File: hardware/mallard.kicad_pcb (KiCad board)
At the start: 2 copper layers, 70 parts, among them J1 USB_A, J2 Conn_02x03_Odd_Even, J3 Conn_01x03, SW1 RESET Switch, U1 TMP235, U10 LTC1983ES6-3, U11 STM32L4Q5xx, U2 TMP235, U3 TMP235, U4 BQ24210DQCT, U5 TMUX1309, U6 TMUX1309, U7 LMP7721, U8 TPS71710DRVR, U9 LMV554

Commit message: Schematic prepared for Layout
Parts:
- added SM1: Conn_01x03, Connector_PinHeader_2.54mm:PinHeader_1x03_P2.54mm_Vertical_SMD_Pin1Right, F.Cu at (24.8, 54.6)
- added SM2: Conn_01x03, Connector_PinHeader_2.54mm:PinHeader_1x03_P2.54mm_Vertical_SMD_Pin1Right, F.Cu at (32.7, 54.6)
- added SM3: Conn_01x03, Connector_PinHeader_2.54mm:PinHeader_1x03_P2.54mm_Vertical_SMD_Pin1Right, F.Cu at (40.7, 54.6)
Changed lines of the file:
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@@
     (tracks 0)
     (zones 0)
-    (modules 70)
+    (modules 73)
     (nets 102)
   )
@@
     (add_net USART1_TX)
   )
+  (module Connector_PinHeader_2.54mm:PinHeader_1x03_P2.54mm_Vertical_SMD_Pin1Right (layer F.Cu)
+    (at 40.665 54.61)
+    (descr "surface-mounted straight pin header, 1x03, 2.54mm pitch, single row, style 2 (pin 1 right)")
+    (tags "Surface mounted pin header SMD 1x03 2.54mm single row style2 pin1 right")
+    (attr smd)
+    (fp_text reference SM3 (at 0 -4.87) (layer F.SilkS)
+      (effects (font (size 1 1) (thickness 0.15)))
+    )
+    (fp_text value Conn_01x03 (at 0 4.87) (layer F.Fab)
+      (effects (font (size 1 1) (thickness 0.15)))
+    )
+    (fp_text user %R (at 0 0 90) (layer F.Fab)
+      (effects (font (size 1 1) (thickness 0.15)))
+    )
+    (fp_line (start 1.27 3.81) (end -1.27 3.81) (layer F.Fab) (width 0.1))
+    (fp_line (start -1.27 -3.81) (end 0.32 -3.81) (layer F.Fab) (width 0.1))
+    (fp_line (start 1.27 3.81) (end 1.27 -2.86) (layer F.Fab) (width 0.1))
+    (fp_line (start 1.27 -2.86) (end 0.32 -3.81) (layer F.Fab) (width 0.1))
+    (fp_line (start -1.27 -3.81) (end -1.27 3.81) (layer F.Fab) (width 0.1))
+    (fp_line (start -1.27 -0.32) (end -2.54 -0.32) (layer F.Fab) (width 0.1))
+    (fp_line (start -2.54 -0.32) (end -2.54 0.32) (layer F.Fab) (width 0.1))
+    (fp_line (start -2.54 0.32) (end -1.27 0.32) (layer F.Fab) (width 0.1))
+    (fp_line (start 1.27 -2.86) (end 2.54 -2.86) (layer F.Fab) (width 0.1))
+    (fp_line (start 2.54 -2.86) (end 2.54 -2.22) (layer F.Fab) (width 0.1))
+    (fp_line (start 2.54 -2.22) (end 1.27 -2.22) (layer F.Fab) (width 0.1))
+    (fp_line (start 1.27 2.22) (end 2.54 2.22) (layer F.Fab) (width 0.1))
+    (fp_line (start 2.54 2.22) (end 2.54 2.86) (layer F.Fab) (width 0.1))
+    (fp_line (start 2.54 2.86) (end 1.27 2.86) (layer F.Fab) (width 0.1))
+    (fp_line (start -1.33 -3.87) (end 1.33 -3.87) (layer F.SilkS) (width 0.12))
+    (fp_line (start -1.33 3.87) (end 1.33 3.87) (layer F.SilkS) (width 0.12))
+    (fp_line (start 1.33 -1.78) (end 1.33 1.78) (layer F.SilkS) (width 0.12))
+    (fp_line (start -1.33 -3.87) (end -1.33 -0.76) (layer F.SilkS) (width 0.12))
+    (fp_line (start 1.33 -3.3) (end 2.85 -3.3) (layer F.SilkS) (width 0.12))
+    (fp_line (start 1.33 -3.87) (end 1.33 -3.3) (layer F.SilkS) (width 0.12))
+    (fp_line (start -1.33 3.3) (end -1.33 3.87) (layer F.SilkS) (width 0.12))
+    (fp_line (start -1.33 0.76) (end -1.33 3.87) (layer F.SilkS) (width 0.12))
+    (fp_line (start -3.45 -4.35) (end -3.45 4.35) (layer F.CrtYd) (width 0.05))
+    (fp_line (start -3.45 4.35) (end 3.45 4.35) (layer F.CrtYd) (width 0.05))
+    (fp_line (start 3.45 4.35) (end 3.45 -4.35) (layer F.CrtYd) (width 0.05))
+    (fp_line (start 3.45 -4.35) (end -3.45 -4.35) (layer F.CrtYd) (width 0.05))
+    (pad 3 smd rect (at 1.655 2.54) (size 2.51 1) (layers F.Cu F.Paste F.Mask)
+      (net 1 GND))
+    (pad 1 smd rect (at 1.655 -2.54) (size 2.51 1) (layers F.Cu F.Paste F.Mask)
+      (net 2 +3V3))
+    (pad 2 smd rect (at -1.655 0) (size 2.51 1) (layers F.Cu F.Paste F.Mask)
+      (net 58 "Net-(SM3-Pad2)"))
+    (model ${KISYS3DMOD}/Connector_PinHeader_2.54mm.3dshapes/PinHeader_1x03_P2.54mm_Vertical_SMD_Pin1Right.wrl
+      (at (xyz 0 0 0))
+      (scale (xyz 1 1 1))
+      (rotate (xyz 0 0 0))
+    )
+  )
+  (module Connector_PinHeader_2.54mm:PinHeader_1x03_P2.54mm_Vertical_SMD_Pin1Right (layer F.Cu)
+    (at 32.715 54.61)
+    (descr "surface-mounted straight pin header, 1x03, 2.54mm pitch, single row, style 2 (pin 1 right)")
+    (tags "Surface mounted pin header SMD 1x03 2.54mm single row style2 pin1 right")
+    (attr smd)
+    (fp_text reference SM2 (at 0 -4.87) (layer F.SilkS)
+      (effects (font (size 1 1) (thickness 0.15)))
+    )
+    (fp_text value Conn_01x03 (at 0 4.87) (layer F.Fab)
+      (effects (font (size 1 1) (thickness 0.15)))
+    )
+    (fp_text user %R (at 0 0 90) (layer F.Fab)
+      (effects (font (size 1 1) (thickness 0.15)))
+    )
+    (fp_line (start 1.27 3.81) (end -1.27 3.81) (layer F.Fab) (width 0.1))
+    (fp_line (start -1.27 -3.81) (end 0.32 -3.81) (layer F.Fab) (width 0.1))
+    (fp_line (start 1.27 3.81) (end 1.27 -2.86) (layer F.Fab) (width 0.1))
+    (fp_line (start 1.27 -2.86) (end 0.32 -3.81) (layer F.Fab) (width 0.1))
+    (fp_line (start -1.27 -3.81) (end -1.27 3.81) (layer F.Fab) (width 0.1))
+    (fp_line (start -1.27 -0.32) (end -2.54 -0.32) (layer F.Fab) (width 0.1))
+    (fp_line (start -2.54 -0.32) (end -2.54 0.32) (layer F.Fab) (width 0.1))
+    (fp_line (start -2.54 0.32) (end -1.27 0.32) (layer F.Fab) (width 0.1))
+    (fp_line (start 1.27 -2.86) (end 2.54 -2.86) (layer F.Fab) (width 0.1))
+    (fp_line (start 2.54 -2.86) (end 2.54 -2.22) (layer F.Fab) (width 0.1))
+    (fp_line (start 2.54 -2.22) (end 1.27 -2.22) (layer F.Fab) (width 0.1))
+    (fp_line (start 1.27 2.22) (end 2.54 2.22) (layer F.Fab) (width 0.1))
+    (fp_line (start 2.54 2.22) (end 2.54 2.86) (layer F.Fab) (width 0.1))
+    (fp_line (start 2.54 2.86) (end 1.27 2.86) (layer F.Fab) (width 0.1))
+    (fp_line (start -1.33 -3.87) (end 1.33 -3.87) (layer F.SilkS) (width 0.12))
+    (fp_line (start -1.33 3.87) (end 1.33 3.87) (layer F.SilkS) (width 0.12))
+    (fp_line (start 1.33 -1.78) (end 1.33 1.78) (layer F.SilkS) (width 0.12))
+    (fp_line (start -1.33 -3.87) (end -1.33 -0.76) (layer F.SilkS) (width 0.12))
+    (fp_line (start 1.33 -3.3) (end 2.85 -3.3) (layer F.SilkS) (width 0.12))
+    (fp_line (start 1.33 -3.87) (end 1.33 -3.3) (layer F.SilkS) (width 0.12))
+    (fp_line (start -1.33 3.3) (end -1.33 3.87) (layer F.SilkS) (width 0.12))
+    (fp_line (start -1.33 0.76) (end -1.33 3.87) (layer F.SilkS) (width 0.12))
+    (fp_line (start -3.45 -4.35) (end -3.45 4.35) (layer F.CrtYd) (width 0.05))
+    (fp_line (start -3.45 4.35) (end 3.45 4.35) (layer F.CrtYd) (width 0.05))
+    (fp_line (start 3.45 4.35) (end 3.45 -4.35) (layer F.CrtYd) (width 0.05))
+    (fp_line (start 3.45 -4.35) (end -3.45 -4.35) (layer F.CrtYd) (width 0.05))
+    (pad 3 smd rect (at 1.655 2.54) (size 2.51 1) (layers F.Cu F.Paste F.Mask)
+      (net 1 GND))
+    (pad 1 smd rect (at 1.655 -2.54) (size 2.51 1) (layers F.Cu F.Paste F.Mask)
+      (net 2 +3V3))
+    (pad 2 smd rect (at -1.655 0) (size 2.51 1) (layers F.Cu F.Paste F.Mask)
+      (net 59 "Net-(SM2-Pad2)"))
+    (model ${KISYS3DMOD}/Connector_PinHeader_2.54mm.3dshapes/PinHeader_1x03_P2.54mm_Vertical_SMD_Pin1Right.wrl
+      (at (xyz 0 0 0))
+      (scale (xyz 1 1 1))
+      (rotate (xyz 0 0 0))
+    )
+  )
+  (module Connector_PinHeader_2.54mm:PinHeader_1x03_P2.54mm_Vertical_SMD_Pin1Right (layer F.Cu)
+    (at 24.765 54.61)
+    (descr "surface-mounted straight pin header, 1x03, 2.54mm pitch, single row, style 2 (pin 1 right)")
+    (tags "Surface mounted pin header SMD 1x03 2.54mm single row style2 pin1 right")
+    (attr smd)
+    (fp_text reference SM1 (at 0 -4.87) (layer F.SilkS)
+      (effects (font (size 1 1) (thickness 0.15)))
+    )
+    (fp_text value Conn_01x03 (at 0 4.87) (layer F.Fab)
+      (effects (font (size 1 1) (thickness 0.15)))
+    )
+    (fp_text user %R (at 0 0 90) (layer F.Fab)
+      (effects (font (size 1 1) (thickness 0.15)))
+    )
+    (fp_line (start 1.27 3.81) (end -1.27 3.81) (layer F.Fab) (width 0.1))
+    (fp_line (start -1.27 -3.81) (end 0.32 -3.81) (layer F.Fab) (width 0.1))
+    (fp_line (start 1.27 3.81) (end 1.27 -2.86) (layer F.Fab) (width 0.1))
+    (fp_line (start 1.27 -2.86) (end 0.32 -3.81) (layer F.Fab) (width 0.1))
+    (fp_line (start -1.27 -3.81) (end -1.27 3.81) (layer F.Fab) (width 0.1))
+    (fp_line (start -1.27 -0.32) (end -2.54 -0.32) (layer F.Fab) (width 0.1))
+    (fp_line (start -2.54 -0.32) (end -2.54 0.32) (layer F.Fab) (width 0.1))
+    (fp_line (start -2.54 0.32) (end -1.27 0.32) (layer F.Fab) (width 0.1))
+    (fp_line (start 1.27 -2.86) (end 2.54 -2.86) (layer F.Fab) (width 0.1))
+    (fp_line (start 2.54 -2.86) (end 2.54 -2.22) (layer F.Fab) (width 0.1))
+    (fp_line (start 2.54 -2.22) (end 1.27 -2.22) (layer F.Fab) (width 0.1))
+    (fp_line (start 1.27 2.22) (end 2.54 2.22) (layer F.Fab) (width 0.1))
+    (fp_line (start 2.54 2.22) (end 2.54 2.86) (layer F.Fab) (width 0.1))
+    (fp_line (start 2.54 2.86) (end 1.27 2.86) (layer F.Fab) (width 0.1))
+    (fp_line (start -1.33 -3.87) (end 1.33 -3.87) (layer F.SilkS) (width 0.12))
+    (fp_line (start -1.33 3.87) (end 1.33 3.87) (layer F.SilkS) (width 0.12))
+    (fp_line (start 1.33 -1.78) (end 1.33 1.78) (layer F.SilkS) (width 0.12))
+    (fp_line (start -1.33 -3.87) (end -1.33 -0.76) (layer F.SilkS) (width 0.12))
+    (fp_line (start 1.33 -3.3) (end 2.85 -3.3) (layer F.SilkS) (width 0.12))
+    (fp_line (start 1.33 -3.87) (end 1.33 -3.3) (layer F.SilkS) (width 0.12))
+    (fp_line (start -1.33 3.3) (end -1.33 3.87) (layer F.SilkS) (width 0.12))
+    (fp_line (start -1.33 0.76) (end -1.33 3.87) (layer F.SilkS) (width 0.12))
+    (fp_line (start -3.45 -4.35) (end -3.45 4.35) (layer F.CrtYd) (width 0.05))
+    (fp_line (start -3.45 4.35) (end 3.45 4.35) (layer F.CrtYd) (width 0.05))
+    (fp_line (start 3.45 4.35) (end 3.45 -4.35) (layer F.CrtYd) (width 0.05))
+    (fp_line (start 3.45 -4.35) (end -3.45 -4.35) (layer F.CrtYd) (width 0.05))
+    (pad 3 smd rect (at 1.655 2.54) (size 2.51 1) (layers F.Cu F.Paste F.Mask)
+      (net 1 GND))
+    (pad 1 smd rect (at 1.655 -2.54) (size 2.51 1) (layers F.Cu F.Paste F.Mask)
+      (net 2 +3V3))
+    (pad 2 smd rect (at -1.655 0) (size 2.51 1) (layers F.Cu F.Paste F.Mask)
+      (net 61 "Net-(SM1-Pad2)"))
+    (model ${KISYS3DMOD}/Connector_PinHeader_2.54mm.3dshapes/PinHeader_1x03_P2.54mm_Vertical_SMD_Pin1Right.wrl
+      (at (xyz 0 0 0))
+      (scale (xyz 1 1 1))
+      (rotate (xyz 0 0 0))
+    )
+  )
   (module Battery:BatteryHolder_Keystone_1042_1x18650 (layer F.Cu)

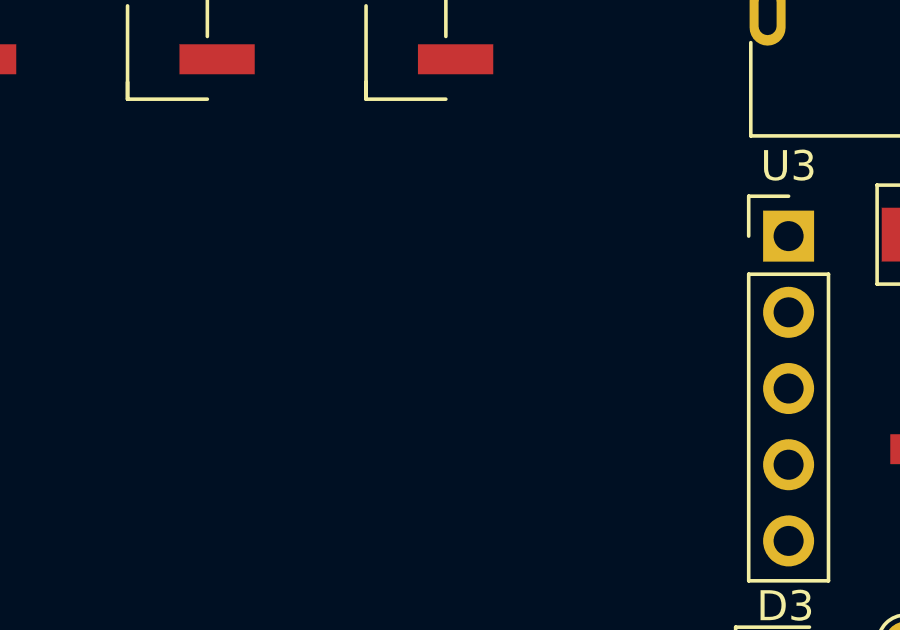
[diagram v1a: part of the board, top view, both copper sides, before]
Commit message: Added screw terminals for solar panel, and added a cap
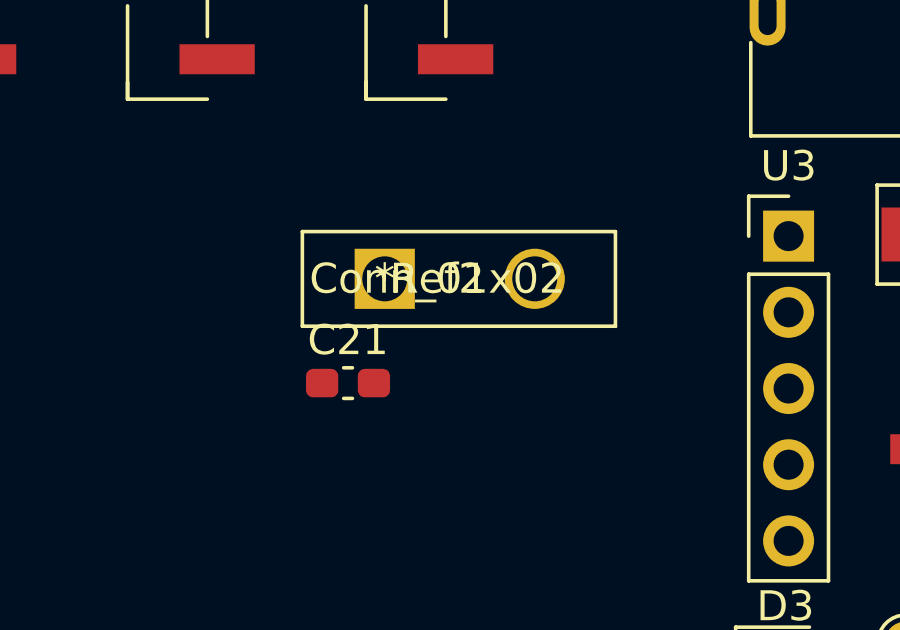
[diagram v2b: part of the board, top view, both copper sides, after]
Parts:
- added C21: 1uF, Capacitor_SMD:C_0603_1608Metric_Pad1.08x0.95mm_HandSolder, F.Cu at (38.7, 67.9)
- added Ref2: Conn_01x02, mallard:mallardScrewTerm., F.Cu at (40.0, 64.5)

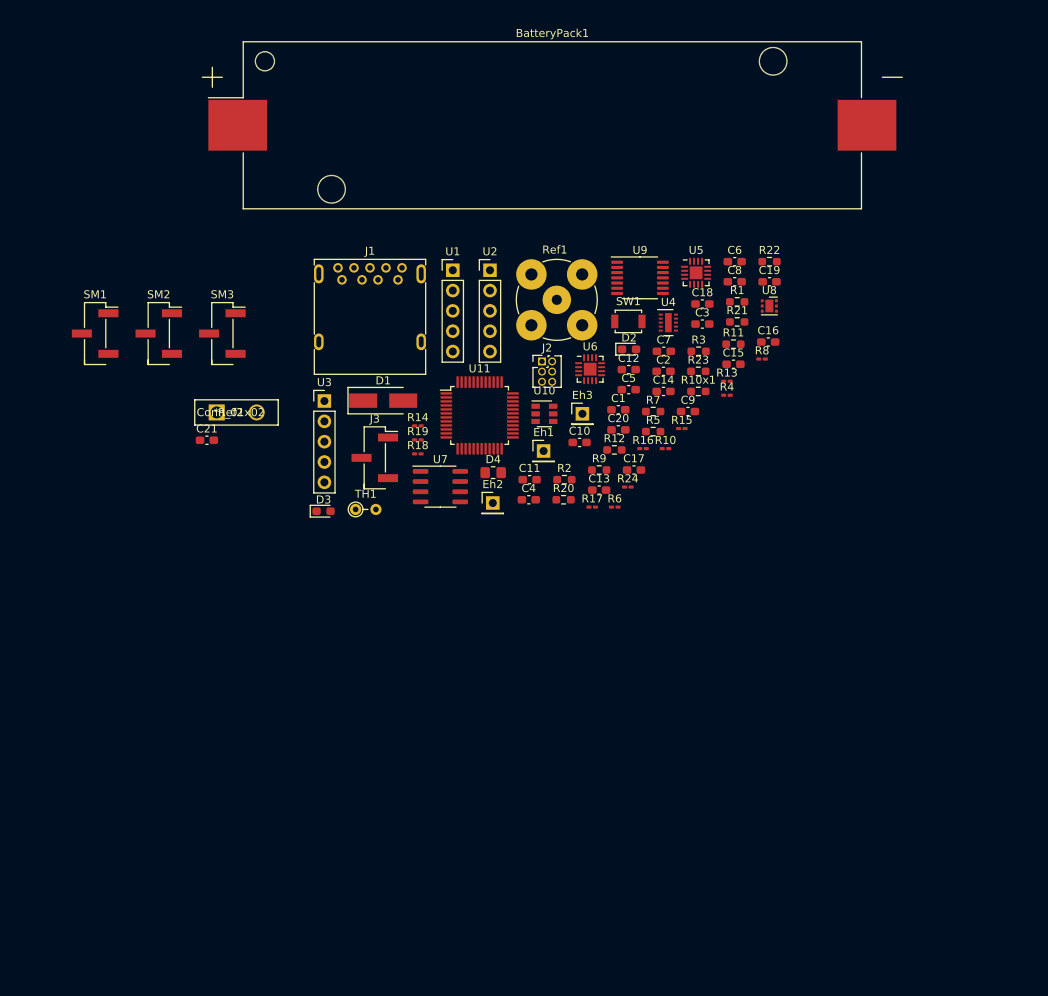
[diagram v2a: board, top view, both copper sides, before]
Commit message: Schematic finished, layout stared
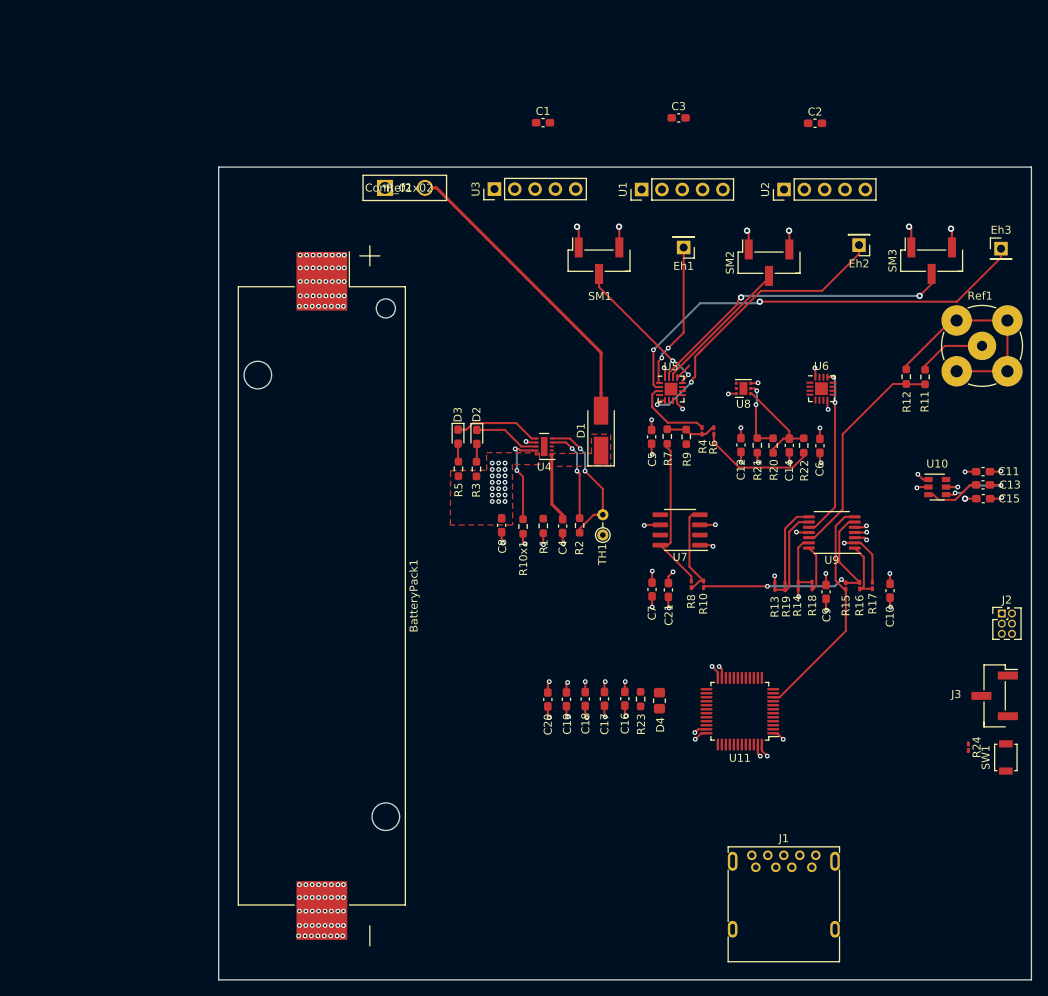
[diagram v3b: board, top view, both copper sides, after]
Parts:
- moved J1 89.8 mm to (107.3, 121.3)
- moved SM3 89.1 mm to (129.3, 45.5), turned to 90 degrees
- moved J3 83.0 mm to (137.2, 99.9)
- moved SM2 76.8 mm to (109.0, 45.8), turned to 90 degrees
- moved SW1 72.1 mm to (138.6, 107.6), turned to 90 degrees
- moved J2 65.5 mm to (138.1, 89.6)
- moved BatteryPack1 65.5 mm to (53.1, 87.4), turned to 270 degrees
- moved SM1 63.6 mm to (87.8, 45.5), turned to 90 degrees
- moved C21 60.6 mm to (96.4, 86.7), turned to 270 degrees
- moved C19 58.0 mm to (83.7, 100.3), turned to 270 degrees
- moved C11 56.7 mm to (135.8, 71.9)
- moved Eh3 56.3 mm to (138.0, 44.0)
- moved Eh2 56.0 mm to (120.2, 43.5), turned to 180 degrees
- moved R24 53.6 mm to (133.9, 106.3), turned to 270 degrees
- moved Ref1 53.5 mm to (135.6, 56.1)
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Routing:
- net Net-(Eh3-Pad1): track 0.00 -> 54.6 mm, vias 0 -> 2
- net GND: track 0.00 -> 51.6 mm, vias 0 -> 75
- net Net-(SM3-Pad2): track 0.00 -> 39.5 mm, vias 0 -> 2
- net +3V3: track 0.00 -> 37.9 mm, vias 0 -> 85
- net Net-(D1-Pad2): track 0.00 -> 37.8 mm
- net Net-(Eh2-Pad1): track 0.00 -> 37.4 mm, vias 0 -> 2
- net Net-(R10-Pad1): track 0.00 -> 29.9 mm, vias 0 -> 2
- net Eh_Sense: track 0.00 -> 29.1 mm
- net Net-(R12-Pad2): track 0.00 -> 28.2 mm
- net Net-(R11-Pad1): track 0.00 -> 28.0 mm
- net Net-(U6-Pad13): track 0.00 -> 21.4 mm, vias 0 -> 2
- net Net-(R7-Pad1): track 0.00 -> 20.1 mm
- net Net-(Eh1-Pad1): track 0.00 -> 18.3 mm, vias 0 -> 2
- net Net-(SM1-Pad2): track 0.00 -> 18.2 mm, vias 0 -> 2
- net Net-(SM2-Pad2): track 0.00 -> 17.7 mm
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- added copper zone on F.Cu, net +3V3
- added copper zone on Power, net +3V3
- added copper zone on Power, net -3V3
- added copper zone on GND, net GND
- added copper zone on F.Cu, net Net-(C4-Pad1)
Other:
- board outline added: 101.6 x 101.6 mm
- copper layers 2 -> 4
